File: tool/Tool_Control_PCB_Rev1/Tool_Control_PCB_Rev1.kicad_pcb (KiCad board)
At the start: 2 copper layers, 14 parts, among them J1 2_pin_phoenix, Q1 MMBT3904, Q2 MMBT3904, Q3 MMBT3904, U1 ESP32-DEVKIT-V1

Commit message: PCB work on out of board connections
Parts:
- added J2: 4_pin_phoenix, Seed_footprints:CONN_1757268_PXC, F.Cu at (160.5, 51.0)
- added J3: 2_pin_phoenix, Seed_footprints:PHOENIX_1757242, F.Cu at (63.4, 29.0)
- added TP7: TestPoint_2Pole, Seed_footprints:Ground_Point, F.Cu at (82.4, 26.2)
- moved U1 0.36 mm to (71.0, 60.5)

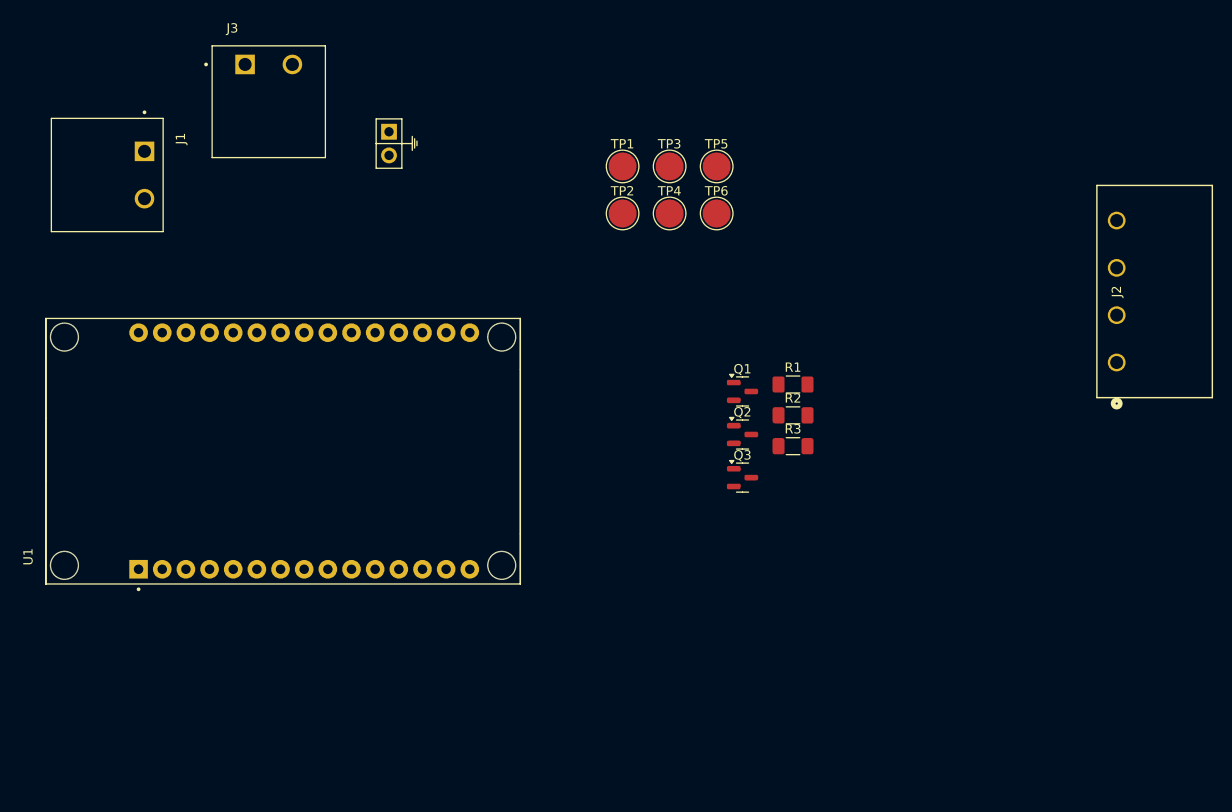
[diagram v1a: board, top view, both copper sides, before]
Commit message: Finished schematic capture and started board layout
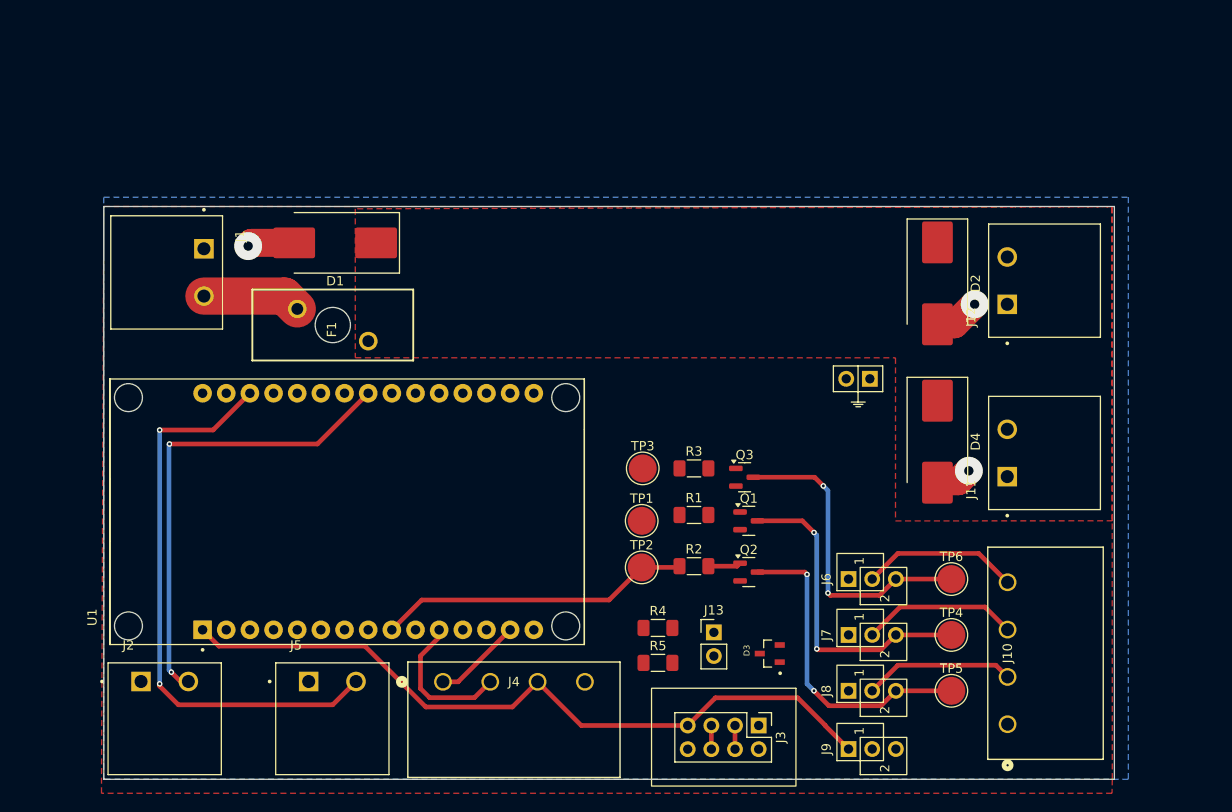
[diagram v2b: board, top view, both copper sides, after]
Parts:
- added D1: D_Schottky, Diode_SMD:D_SMC_Handsoldering, F.Cu at (76.6, 38.2)
- added D2: D_Schottky, Diode_SMD:D_SMC_Handsoldering, F.Cu at (141.2, 42.5)
- added D3: MMBZ5226B-7-F, Seed_footprints:SOT91P240X102-3N, F.Cu at (123.2, 82.2)
- added D4: D_Schottky, Diode_SMD:D_SMC_Handsoldering, F.Cu at (141.2, 59.5)
- added F1: Fuse, Seed_footprints:01530008 (FuseHold), F.Cu at (76.3, 47.0)
- added J10: 4_pin_phoenix, Seed_footprints:CONN_1757268_PXC, F.Cu at (148.8, 89.8)
- added J11: 2_pin_phoenix, Seed_footprints:PHOENIX_1757242, F.Cu at (158.8, 66.8)
- added J12: 2_pin_phoenix, Seed_footprints:PHOENIX_1757242, F.Cu at (158.8, 48.3)
- added J13: Conn_01x02_Pin, Connector_PinHeader_2.54mm:PinHeader_1x02_P2.54mm_Vertical, F.Cu at (117.2, 80.0)
- added J4: 4_pin_phoenix, Seed_footprints:CONN_1757268_PXC, F.Cu at (88.2, 85.3)
- added J5: 2_pin_phoenix, Seed_footprints:PHOENIX_1757242, F.Cu at (70.2, 95.2)
- added J6: Cut Trace/Jumper, Seed_footprints:Jumper Selector, F.Cu at (131.7, 74.2)
- added J7: Cut Trace/Jumper, Seed_footprints:Jumper Selector, F.Cu at (131.7, 80.2)
- added J8: Cut Trace/Jumper, Seed_footprints:Jumper Selector, F.Cu at (131.7, 86.2)
- added J9: Cut Trace/Jumper, Seed_footprints:Jumper Selector, F.Cu at (131.7, 92.5)
- added R4: R, Resistor_SMD:R_1206_3216Metric_Pad1.30x1.75mm_HandSolder, F.Cu at (111.2, 79.5)
- added R5: R, Resistor_SMD:R_1206_3216Metric_Pad1.30x1.75mm_HandSolder, F.Cu at (111.2, 83.2)
- J2: value 4_pin_phoenix -> 2_pin_phoenix; footprint Seed_footprints:CONN_1757268_PXC -> Seed_footprints:PHOENIX_1757242
- J3: value 2_pin_phoenix -> Conn_02x04_Odd_Even; footprint Seed_footprints:PHOENIX_1757242 -> Connector_PinHeader_2.54mm:PinHeader_2x04_P2.54mm_Vertical
- moved J2 117.0 mm to (52.2, 95.2), turned to 0 degrees
- moved J3 84.6 mm to (122.1, 90.0), turned to -90 degrees
- moved TP5 61.7 mm to (142.8, 86.2)
- moved TP7 58.0 mm to (134.0, 52.8), turned to -90 degrees
- moved TP4 54.4 mm to (142.8, 80.2)
- moved TP6 46.6 mm to (142.8, 74.2)
- moved TP1 38.1 mm to (109.5, 68.0)
- moved TP2 38.1 mm to (109.5, 73.0)
- moved TP3 32.5 mm to (109.6, 62.4)
- moved R2 19.4 mm to (115.1, 72.9)
- moved R1 17.6 mm to (115.1, 67.4)
- moved Q2 14.8 mm to (121.0, 73.5)
- moved Q1 13.9 mm to (121.0, 68.0)
- moved J1 12.3 mm to (52.5, 35.2)
- moved R3 10.9 mm to (115.1, 62.4)
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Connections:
- J1 pad 02: +12V -> Net-(F1-Pad1)
- U1 pad 1: unconnected-(U1-3V3-Pad1) -> +3.3V
- U1 pad 11: unconnected-(U1-D21-Pad11) -> /TOF_sensor_SDA
- U1 pad 14: unconnected-(U1-D22-Pad14) -> /TOF_sensor_SCL
- U1 pad 15: unconnected-(U1-D23-Pad15) -> /ALT_tool_stepper_en
- U1 pad 19: unconnected-(U1-D34-Pad19) -> /current_sense_MCU
- U1 pad 21: unconnected-(U1-D32-Pad21) -> /drill_en
- U1 pad 23: unconnected-(U1-D25-Pad23) -> /home_switch
- U1 pad 24: unconnected-(U1-D26-Pad24) -> /drill_CW
- U1 pad 25: unconnected-(U1-D27-Pad25) -> /drill_CCW
- U1 pad 28: unconnected-(U1-D13-Pad28) -> /TOF_sensor_~{INT}
- U1 pad 6: unconnected-(U1-RX2-Pad6) -> /ALT_tool_stepper_step
- U1 pad 7: unconnected-(U1-TX2-Pad7) -> /ALT_tool_stepper_dir
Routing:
- net +3.3V: track 0.00 -> 79.4 mm
- net /TOF_sensor_~{INT}: track 0.00 -> 61.8 mm, vias 0 -> 2
- net /home_switch: track 0.00 -> 50.5 mm, vias 0 -> 2
- net /output_tool_step_dir: track 0.00 -> 34.4 mm, vias 0 -> 2
- net /output_tool_stepper_step: track 0.00 -> 34.3 mm, vias 0 -> 2
- net /UC_tool_stepper_step: track 0.00 -> 33.7 mm
- net /output_tool_stepper_en: track 0.00 -> 33.7 mm, vias 0 -> 2
- net /Stepper EN: track 0.00 -> 17.0 mm
- net /Stepper Dir: track 0.00 -> 16.8 mm
- net /Stepper Step: track 0.00 -> 16.2 mm
- net /TOF_sensor_SDA: track 0.00 -> 15.7 mm
- net GND: track 0.00 -> 13.4 mm, vias 0 -> 3
- net Net-(F1-Pad1): track 0.00 -> 10.6 mm
- net /TOF_sensor_SCL: track 0.00 -> 9.53 mm
- net Net-(Q2-B): track 0.00 -> 3.53 mm
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- added copper zone on F.Cu, net +12V
- added copper zone on B.Cu, net GND
- added copper zone on F.Cu, net GND
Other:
- board outline added: 108.5 x 61.5 mm
- board text added: "3.3"
- board text added: "CHECK ROTATION OF THIS PORT"
- board text added: "Home SW"
- board text added: "Is"
- board text added: "SCL"
- board text added: "SDA"

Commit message: pre review board
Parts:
- added G***: LOGO, LOGO, F.Cu at (130.0, 39.5)
- added U2: ~, Seed_footprints:M3 bolt, F.Cu at (89.0, 67.5)
- added U3: ~, Seed_footprints:M3 bolt, F.Cu at (133.5, 67.0)
- added U4: ~, Seed_footprints:M3 bolt, F.Cu at (121.0, 55.5)
- added U5: ~, Seed_footprints:M3 bolt, F.Cu at (66.5, 67.5)
- D1, D2, D4: value D_Schottky -> SK810L-TP
- moved J3 8.01 mm to (114.5, 92.5), turned to 90 degrees
- moved D3 3.25 mm to (123.2, 79.0)
- moved J13 1.97 mm to (117.2, 78.0)
- moved R5 1.06 mm to (112.0, 82.5)
- moved R4 0.56 mm to (111.2, 78.9), turned to 180 degrees
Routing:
- net /drill_CCW: track 0.00 -> 100.6 mm, vias 0 -> 2
- net /UC_tool_step_dir: track 0.00 -> 80.6 mm, vias 0 -> 3
- net /ALT_tool_stepper_step: track 0.00 -> 78.7 mm, vias 0 -> 4
- net /drill_CW: track 0.00 -> 75.6 mm, vias 0 -> 2
- net /UC_tool_stepper_en: track 0.00 -> 75.3 mm, vias 0 -> 3
- net /ALT_tool_stepper_dir: track 0.00 -> 73.1 mm, vias 0 -> 5
- net /drill_en: track 2.54 -> 65.1 mm, vias 0 -> 3
- net /current_sense_MCU: track 0.00 -> 55.0 mm, vias 0 -> 2
- net +12V: track 0.00 -> 40.9 mm
- net /ALT_tool_stepper_en: track 0.00 -> 38.4 mm, vias 0 -> 2
- net /current_sense: track 2.54 -> 20.7 mm, vias 0 -> 1
- net /Stepper COM+: track 0.00 -> 15.6 mm
- net Net-(J13-Pin_2): track 0.00 -> 13.3 mm
- net Net-(Q1-B): track 0.00 -> 3.53 mm
- net GND: track 13.4 -> 16.9 mm, vias 3 -> 4
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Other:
- board text added: "12 Volt"
- board text added: "CHECK Bolt tols!"
- board text added: "Front Tool Interface Board Board Engineer: Niels Keller"
- board text added: "Power In 12V"
- board text added: "Seed Team: 485 A. Brown, N. Keller, C. Larcom, J Poirier"
- board text added: "TOF"
- board text removed: "CHECK ROTATION OF THIS PORT"

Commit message: rev 0 draft
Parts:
- moved U2 0.50 mm to (89.0, 67.0)
- moved U5 0.50 mm to (66.5, 67.0)
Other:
- outline, holes or cut-outs redrawn
- board text added: "BBJ was here"
- board text added: "Rev. 0 2/20/2026"
- board text removed: "CHECK Bolt tols!"

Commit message: Submittion of board
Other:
- board text added: "WayWayWay"
- board text removed: "BBJ was here"
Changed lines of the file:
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@@
 		)
 	)
-	(gr_text "BBJ was here"
-		(at 73.5 68 0)
+	(gr_text "WayWayWay"
+		(at 72 67 0)
 		(layer "F.SilkS")
 		(effects
 			(font
-				(size 1 1)
-				(thickness 0.1)
+				(size 1.5 1.5)
+				(thickness 0.3)
+				(bold yes)
 			)
 			(justify left bottom)
